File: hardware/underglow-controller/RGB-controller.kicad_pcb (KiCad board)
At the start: 4 copper layers, 86 x 97.7 mm, 175 parts, among them J2 U.FL-R-SMT-1(10), J3 DM3AT-SF-PEJM5, J4 DTM1312PA12PBR008, J5 Conn_01x10, J6 CONSOLE, J7 U.FL-R-SMT-1(10), J8 JTAG, J9 Conn_01x10, Q2 STS8DNF3LL, Q3 STS8DNF3LL, Q4 STS8DNF3LL, Q5 MBT3904DW1T1G, Q6 MBT3904DW1T1G, SW2 SW_Push, SW3 SW_Push, SW4 SW_Push, SW5 SW_Push, U10 DRV8844PWP, U11 RP2040, U2 SX1231HIMLTRT, U3 SN65HVD230, U4 ESP32-S3R2, U5 W25Q128JVS, U6 WS2815B, U7 W25Q128JVS, U8 ADP2303ARDZ-3.3, Y2 40MHZ, Y3 32.7k, Y4 12MHZ, Y5 32.7k

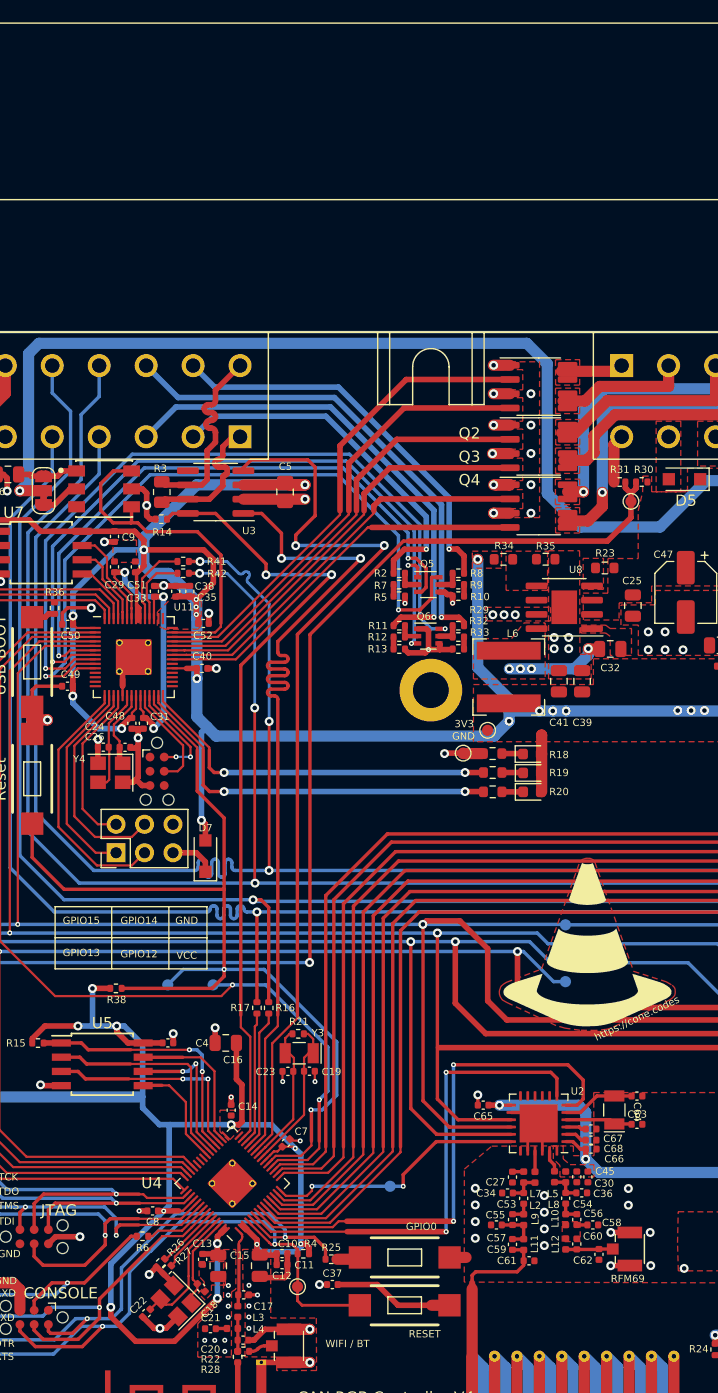
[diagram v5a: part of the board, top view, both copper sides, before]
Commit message: start to break into sheets
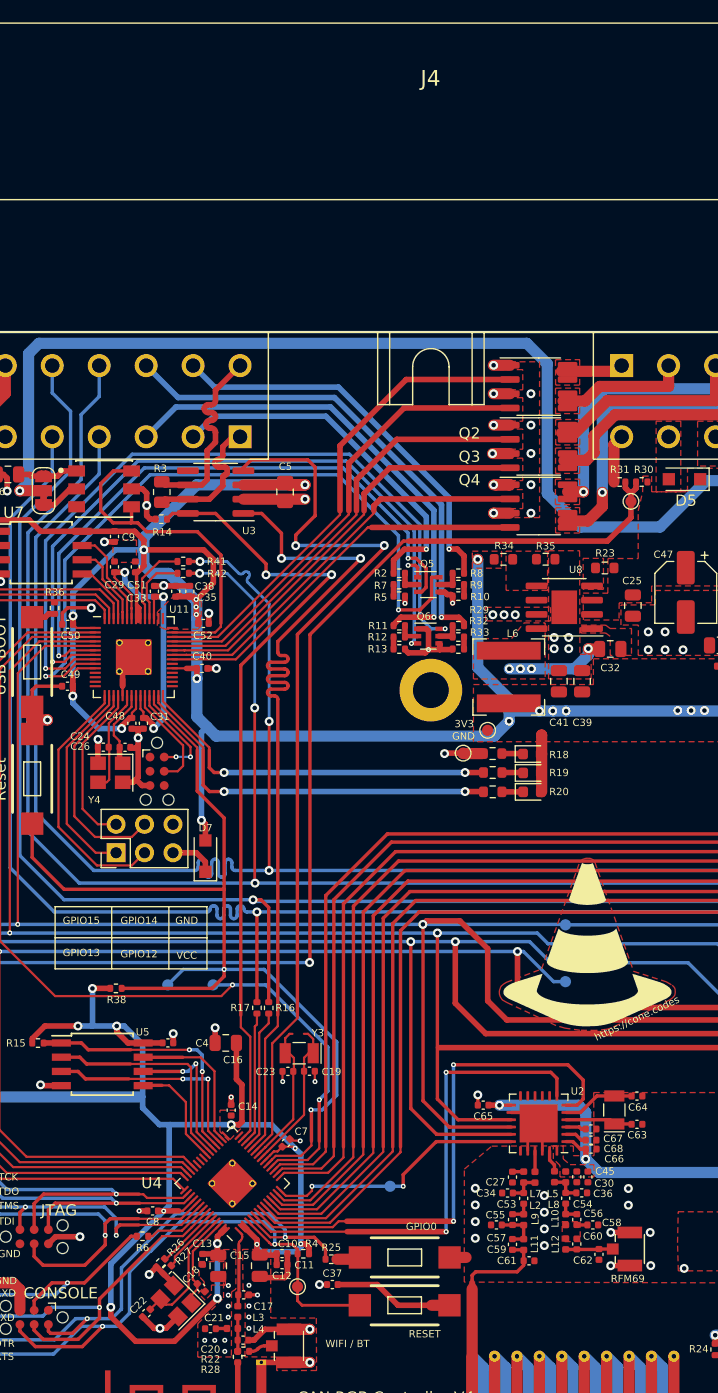
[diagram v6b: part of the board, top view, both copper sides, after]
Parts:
- removed R21: DNP, Resistor_SMD:R_0402_1005Metric
- C38: value 1uF -> 0.1uF
- C51: value 0.1uF -> 1uF
- D3: value RED -> GRN
- D4: value GRN -> RED
- D7: value D_Small -> CUHS15S30,H3F
- J9: value Conn_01x10 -> Spare IO
- SW4: value SW_Push -> USB BOOT
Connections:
- net /LED_GREEN renamed /Pico Remote Proc/LED_GREEN
- net /LED_RED renamed /Pico Remote Proc/LED_RED
- net /RP_GPIO12 renamed /Pico Remote Proc/RP_GPIO12
- net /RP_GPIO13 renamed /Pico Remote Proc/RP_GPIO13
- net /RP_GPIO14 renamed /Pico Remote Proc/RP_GPIO14
- net /RP_GPIO15 renamed /Pico Remote Proc/RP_GPIO15
- net /RP_SCLK renamed /Pico Remote Proc/RP_SCLK
- net /RP_SD0 renamed /Pico Remote Proc/RP_SD0
- net /RP_SD1 renamed /Pico Remote Proc/RP_SD1
- net /RP_SD2 renamed /Pico Remote Proc/RP_SD2
- net /RP_SD3 renamed /Pico Remote Proc/RP_SD3
- net /RP_SS renamed /Pico Remote Proc/RP_SS
- net /RP_SWCLK renamed /Pico Remote Proc/RP_SWCLK
- net /RP_SWD renamed /Pico Remote Proc/RP_SWD
- net /RP_USB_D_M renamed /Pico Remote Proc/RP_USB_D_N
- net /RP_USB_D_P renamed /Pico Remote Proc/RP_USB_D_P
- net /USB_BOOT renamed /Pico Remote Proc/USB_BOOT
- C24 pad 1: /RP_XOUT -> /Pico Remote Proc/RP_XOUT
- C26 pad 1: /RP_XIN -> /Pico Remote Proc/RP_XIN
- D3 pad 1: Net-(D3-Pad1) -> Net-(R20-Pad1)
- D4 pad 1: Net-(D4-Pad1) -> Net-(R19-Pad1)
- R19 pad 1: Net-(D3-Pad1) -> Net-(R19-Pad1)
- R20 pad 1: Net-(D4-Pad1) -> Net-(R20-Pad1)
- U11 pad 20: /RP_XIN -> /Pico Remote Proc/RP_XIN
- U11 pad 21: /RP_XOUT -> /Pico Remote Proc/RP_XOUT
- U11 pad 39: /GPIO_GPO2 -> /GPIO_GPO1
- U11 pad 40: /GPIO_GPO1 -> /GPIO_GPO2
- Y4 pad 1: /RP_XOUT -> /Pico Remote Proc/RP_XIN
- Y4 pad 3: /RP_XIN -> /Pico Remote Proc/RP_XOUT
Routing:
- net /RP_XIN: track 9.21 -> 0.00 mm
- net /Pico Remote Proc/RP_XIN: track 0.00 -> 9.21 mm
- net /RP_XOUT: track 6.62 -> 0.00 mm
- net /Pico Remote Proc/RP_XOUT: track 0.00 -> 6.62 mm
- net Net-(R20-Pad1): track 0.00 -> 3.40 mm
- net /GPIO_GPO2: track 41.4 -> 43.6 mm
- net /GPIO_GPO1: track 43.6 -> 41.4 mm
- net Net-(D4-Pad1): track 1.72 -> 0.00 mm
- net Net-(D3-Pad1): track 1.68 -> 0.00 mm

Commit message: pcb updates
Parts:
- removed C28: 1uF, Capacitor_SMD:C_0402_1005Metric
- removed C68: 0.1uF, Capacitor_SMD:C_0402_1005Metric
- removed D6: D_Small, Diode_SMD:D_SOD-123F
- removed J3: DM3AT-SF-PEJM5, ConeCodes:HRS_DM3AT-SF-PEJM5
- removed J5: Conn_01x10, Connector_PinHeader_2.54mm:PinHeader_1x10_P2.54mm_Vertical
- removed J8: JTAG, Connector_PinHeader_1.27mm:PinHeader_1x05_P1.27mm_Vertical
- removed R24, R40, R43, R44, R45: 10k, Resistor_SMD:R_0402_1005Metric
- removed TC4: TC2030-IDC, Connector:Tag-Connect_TC2030-IDC-NL_2x03_P1.27mm_Vertical
- added C2: 10uF, Capacitor_SMD:C_0805_2012Metric, F.Cu at (82.4, 116.6)
- added C3: 16pF, Capacitor_SMD:C_0402_1005Metric, F.Cu at (80.0, 114.8)
- added J10: U.FL-R-SMT-1(10), ConeCodes:HRS_U.FL-R-SMT-1(10), F.Cu at (96.0, 100.8)
- added REF**: Wuerth_36103305_30x30mm, RF_Shielding:Wuerth_36103305_30x30mm, F.Cu at (84.7, 121.2)
- added TP13: DIO0, TestPoint:TestPoint_Pad_D1.0mm, F.Cu at (72.3, 122.8)
- added TP14: DIO1, TestPoint:TestPoint_Pad_D1.0mm, F.Cu at (73.9, 123.7)
- added TP15: DIO2, TestPoint:TestPoint_Pad_D1.0mm, F.Cu at (72.3, 124.4)
- added TP16: DIO3, TestPoint:TestPoint_Pad_D1.0mm, F.Cu at (73.9, 125.3)
- added TP17: DIO4, TestPoint:TestPoint_Pad_D1.0mm, F.Cu at (72.3, 126.0)
- added TP18: DIO5, TestPoint:TestPoint_Pad_D1.0mm, F.Cu at (73.9, 126.9)
- AE3: value PCB_ANT_RFM69 -> Antenna_Shield
- C27, C30, C36, C45: value C_Small -> 0.1uF
- C34: value C_Small -> 16pF
- C54: value C_Small -> 0.01uF
- C55: value C_Small -> 68pF
- C56, C59: value C_Small -> 8.2pF
- C58: value C_Small -> 22pF
- C62: value C_Small -> 6.8pF
- C63: value 10pF -> 6.8pF
- C64: value 10pF -> C_Small
- C65: value 0.1uF -> C_Small
- C66: value 0.1uF -> 3.3pF
- C67: value 0.1uF -> 5.6pF
- D3: value GRN -> RED
- D4: value RED -> GRN
- L10, L12: value L_Small -> 6.8nH
- L11, L9: value L_Small -> 5.6nH
- L2: value L_Small -> 2.7nH
- L5: value L_Small -> 3.9nH
- L7: value L_Small -> 22nH
- L8: value L_Small -> 33nH
- TP10, TP11, TP12: moved to F.Cu
- TP3: value VBAT_SENSE -> VSENSE
- U2: footprint Package_DFN_QFN:QFN-24-1EP_5x5mm_P0.65mm_EP3.4x3.4mm -> Package_DFN_QFN:QFN-24-1EP_5x5mm_P0.65mm_EP3.4x3.4mm_ThermalVias
- Y5: value 32.7k -> 32mhz; footprint Crystal:Crystal_SMD_MicroCrystal_CC7V-T1A-2Pin_3.2x1.5mm -> Crystal:Crystal_SMD_2520-4Pin_2.5x2.0mm
- moved C65 26.0 mm to (91.5, 127.8)
- moved AE3 25.5 mm to (103.7, 124.0), turned to -90 degrees
- moved J2 24.0 mm to (90.9, 100.7), turned to 0 degrees
- moved C67 18.3 mm to (93.1, 127.1), turned to -90 degrees
- moved L11 16.3 mm to (91.5, 121.9), turned to 0 degrees
- moved C63 14.2 mm to (90.0, 126.2), turned to 90 degrees
- moved C64 14.2 mm to (91.5, 123.0), turned to 180 degrees
- moved C66 14.0 mm to (93.1, 122.5), turned to 90 degrees
- moved L9 13.3 mm to (88.5, 123.0), turned to 0 degrees
- moved C57 13.1 mm to (85.1, 126.2), turned to 90 degrees
- moved C61 13.0 mm to (88.5, 127.7), turned to 180 degrees
- moved L12 12.9 mm to (91.5, 126.6), turned to 0 degrees
- moved AE2 12.9 mm to (36.9, 133.9)
- moved C59 12.7 mm to (86.6, 126.6), turned to 0 degrees
- moved U2 12.6 mm to (79.1, 125.0), turned to -90 degrees
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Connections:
- net /BST renamed /Power/BST
- net /CHIP_PU renamed /ESP32-S3/CHIP_PU
- net /CP1 renamed /Motor-Control/CP1
- net /CP2 renamed /Motor-Control/CP2
- net /DRV_RESET renamed /MCPWM_RESET
- net /DRV_SLEEP renamed /MCPWM_SLEEP
- net /EN1 renamed /MCPWM0_ENA
- net /EN2 renamed /MCPWM0_ENB
- net /EN3 renamed /MCPWM1_ENA
- net /EN4 renamed /MCPWM1_ENB
- net /FB renamed /Power/FB
- net /FSPICLK renamed /SCLK
- net /FSPICS0 renamed /ESP32-S3/FSPICS0
- net /FSPICS1 renamed /CS1
- net /FSPICS2 renamed /CS2
- net /FSPID renamed /MOSI
- net /FSPIQ renamed /MISO
- net /GPI1 renamed /Connectors/GPI1
- net /GPI2 renamed /Connectors/GPI2
- net /GPI3 renamed /Connectors/GPI3
- net /GPI4 renamed /Connectors/GPI4
- net /GPIO0_BOOTSTRAP renamed /ESP32-S3/GPIO0_BOOTSTRAP
- net /GPIO1 renamed /SX1276_IRQ
- net /GPIO10 renamed /MCPWM1_INB
- net /GPIO14 renamed /RP2040_EN
- net /GPIO2 renamed /SX1276_RESET
- net /GPIO21 renamed /CAN_EN
- net /GPIO3 renamed /MCPWM0_INA
- net /GPIO38 renamed /VSENSE
- net /GPIO5 renamed /MCPWM0_INB
- net /GPIO7 renamed /MCPWM1_INA
- net /GPIO_USB_D_N renamed /ESP32-S3/GPIO19
- net /GPIO_USB_D_P renamed /ESP32-S3/GPIO20
- net /GPO1 renamed /Connectors/GPO1
- net /GPO2 renamed /Connectors/GPO2
- net /GPO3 renamed /Connectors/GPO3
- net /GPO4 renamed /Connectors/GPO4
- net /GPO5 renamed /Connectors/GPO5
- net /GPO6 renamed /Connectors/GPO6
- net /LEDA_OUT renamed /External-IO/LEDA_OUT
- net /LNA_IN renamed /ESP32-S3/LNA_IN
- net /MOTOR1_OUT1 renamed /Connectors/MOTOR1_OUT1
- net /MOTOR1_OUT2 renamed /Connectors/MOTOR1_OUT2
- net /PGOOD renamed /Power/PGOOD
- net /RF_ANT renamed /ESP32-S3/RF_ANT
- net /RF_ANT_EXT renamed /ESP32-S3/RF_ANT_EXT
- net /RTC_XTAL_N renamed /ESP32-S3/RTC_XTAL_N
- net /RTC_XTAL_P renamed /ESP32-S3/RTC_XTAL_P
- net /RXD renamed /ESP32-S3/RXD
- net /SPICLK renamed /ESP32-S3/SPICLK
- net /SPICS0 renamed /ESP32-S3/SPICS0
- net /SPICS1 renamed /ESP32-S3/SPICS1
- net /SPID renamed /ESP32-S3/SPID
- net /SPIHD renamed /ESP32-S3/SPIHD
- net /SPIQ renamed /ESP32-S3/SPIQ
- net /SPIWP renamed /ESP32-S3/SPIWP
- net /SW renamed /Power/SW
- net /TXD renamed /ESP32-S3/TXD
- net /WS2815B_VCC renamed /External-IO/WS2815B_VCC
- net /WS2815B_VDD renamed /External-IO/WS2815B_VDD
- net /XTAL_N renamed /ESP32-S3/XTAL_N
- net /XTAL_P renamed /ESP32-S3/XTAL_P
- net Net-(C42-Pad1) renamed /Motor-Control/V3P3OUT
- net Net-(C43-Pad1) renamed /Motor-Control/VCP
- AE3 pad 1: /RF69_RF_ANT_PCB -> unconnected-(AE3-Pad1)
- C27 pad 1: Net-(C27-Pad1) -> +3V3
- C30 pad 1: /VR_PA -> +3V3
- C34 pad 1: Net-(C34-Pad1) -> /SX1276/RADIO_XTAL_N
- C36 pad 1: Net-(C36-Pad1) -> /SX1276/VR_DIG
- C45 pad 1: /VR_PA -> /SX1276/VR_ANA
- C53 pad 1: Net-(C34-Pad1) -> /SX1276/VR_PA
- C53 pad 2: Net-(C53-Pad2) -> GND
- C54 pad 1: Net-(C36-Pad1) -> /SX1276/VR_PA
- C54 pad 2: Net-(C54-Pad2) -> GND
- C55 pad 1: Net-(C53-Pad2) -> /SX1276/VR_PA
- C55 pad 2: Net-(C55-Pad2) -> GND
- C56 pad 1: Net-(C54-Pad2) -> Net-(C56-Pad1)
- C56 pad 2: Net-(C56-Pad2) -> GND
- C57 pad 1: Net-(C55-Pad2) -> Net-(C57-Pad1)
- C58 pad 1: Net-(C56-Pad2) -> Net-(C56-Pad1)
- C58 pad 2: GND -> Net-(C58-Pad2)
- C59 pad 1: Net-(C55-Pad2) -> Net-(C57-Pad1)
- C59 pad 2: /RF69_RF_ANT_PCB -> Net-(C59-Pad2)
- C60 pad 1: Net-(C56-Pad2) -> Net-(C60-Pad1)
- C60 pad 2: /RF69_RF_EXT -> Net-(C58-Pad2)
- C61 pad 1: /RF69_RF_ANT_PCB -> Net-(C61-Pad1)
- C61 pad 2: GND -> Net-(C59-Pad2)
- C62 pad 1: /RF69_RF_EXT -> Net-(C60-Pad1)
- C63 pad 1: /RADIO_XTAL_P -> Net-(C61-Pad1)
- C64 pad 1: /RADIO_XTAL_N -> Net-(C64-Pad1)
- C64 pad 2: GND -> Net-(C60-Pad1)
- C65 pad 1: +3V3 -> Net-(C65-Pad1)
- C65 pad 2: GND -> Net-(C61-Pad1)
- C66 pad 1: +3V3 -> Net-(C64-Pad1)
- C67 pad 1: /VR_DIG -> Net-(C65-Pad1)
- D3 pad 1: Net-(R20-Pad1) -> Net-(D3-Pad1)
- D4 pad 1: Net-(R19-Pad1) -> Net-(D4-Pad1)
- J2 pad 2: /RF69_RF_EXT -> Net-(C64-Pad1)
- J4 pad A10: /MOTOR2_OUT2 -> /Connectors/MOTOR2_OUT2
- J4 pad A9: /MOTOR2_OUT1 -> /Connectors/MOTOR2_OUT1
- J4 pad B4: /CONN_RP_USB_D_P -> unconnected-(J4-PadB4)
- J4 pad B5: /USB_D_P -> unconnected-(J4-PadB5)
- J4 pad B7: /V33OUT -> unconnected-(J4-PadB7)
- J4 pad B8: /USB_D_N -> unconnected-(J4-PadB8)
- J4 pad B9: /CONN_RP_USB_D_N -> unconnected-(J4-PadB9)
- J6 pad 5: /CTS -> /ESP32-S3/CTS
- L10 pad 1: Net-(C54-Pad2) -> Net-(C59-Pad2)
- L10 pad 2: Net-(C56-Pad2) -> Net-(C61-Pad1)
- L11 pad 1: Net-(C55-Pad2) -> Net-(C60-Pad1)
- L11 pad 2: /RF69_RF_ANT_PCB -> Net-(C64-Pad1)
- L12 pad 1: Net-(C56-Pad2) -> Net-(C61-Pad1)
- L12 pad 2: /RF69_RF_EXT -> Net-(C65-Pad1)
- L2 pad 1: /RFIO -> /SX1276/PA_BOOST
- L2 pad 2: Net-(C34-Pad1) -> Net-(C56-Pad1)
- L5 pad 1: /PA_BOOST -> /SX1276/RFIO
- L5 pad 2: Net-(C36-Pad1) -> Net-(C57-Pad1)
- L7 pad 1: Net-(C27-Pad1) -> /SX1276/VR_PA
- L7 pad 2: Net-(C34-Pad1) -> Net-(C56-Pad1)
- L8 pad 1: /VR_PA -> /SX1276/VR_PA
- L8 pad 2: Net-(C36-Pad1) -> Net-(C57-Pad1)
- L9 pad 1: Net-(C53-Pad2) -> Net-(C58-Pad2)
- L9 pad 2: Net-(C55-Pad2) -> Net-(C60-Pad1)
- R16 pad 2: /USB_D_N -> /Connectors/USB_D_P
- R17 pad 2: /USB_D_P -> /Connectors/USB_D_N
- R19 pad 1: Net-(R19-Pad1) -> Net-(D3-Pad1)
- R20 pad 1: Net-(R20-Pad1) -> Net-(D4-Pad1)
- R25 pad 1: /CTS -> /ESP32-S3/CTS
- R26 pad 1: /GPIO45 -> /ESP32-S3/GPIO45
- R27 pad 1: /GPIO46 -> /ESP32-S3/GPIO46
- R41 pad 1: /CONN_RP_USB_D_P -> /Connectors/CONN_RP_USB_D_P
- R42 pad 1: /CONN_RP_USB_D_N -> /Connectors/CONN_RP_USB_D_N
- TC2 pad 2: /CTS -> /ESP32-S3/CTS
- U10 pad 10: /MOTOR2_OUT2 -> /Connectors/MOTOR2_OUT1
- U10 pad 18: unconnected-(U10-Pad18) -> /MCPWM_FAULT
- U10 pad 8: /MOTOR2_OUT1 -> /Connectors/MOTOR2_OUT2
- U11 pad 39: /GPIO_GPO1 -> /GPIO_GPO2
- U11 pad 40: /GPIO_GPO2 -> /GPIO_GPO1
- U2 pad 10: unconnected-(U2-Pad10) -> /SX1276/DIO3
- U2 pad 11: unconnected-(U2-Pad11) -> /SX1276/DIO4
- U2 pad 12: unconnected-(U2-Pad12) -> /SX1276/DIO5
- U2 pad 2: /VR_ANA -> /SX1276/VR_ANA
- U2 pad 21: /RFIO -> /SX1276/RFIO
- U2 pad 23: /PA_BOOST -> /SX1276/PA_BOOST
- U2 pad 24: /VR_PA -> /SX1276/VR_PA
- U2 pad 3: /VR_DIG -> /SX1276/VR_DIG
- U2 pad 4: /RADIO_XTAL_P -> /SX1276/RADIO_XTAL_P
- U2 pad 5: /RADIO_XTAL_N -> /SX1276/RADIO_XTAL_N
- U2 pad 8: unconnected-(U2-Pad8) -> /SX1276/DIO1
- U2 pad 9: unconnected-(U2-Pad9) -> /SX1276/DIO2
- U4 pad 44: /MTCK -> /ESP32-S3/MTCK
- U4 pad 45: /MTDO -> /ESP32-S3/MTDO
- U4 pad 47: /MTDI -> /ESP32-S3/MTDI
- U4 pad 48: /MTMS -> /ESP32-S3/MTMS
- U4 pad 5: /CTS -> unconnected-(U4-Pad5)
- U4 pad 51: /GPIO45 -> unconnected-(U4-Pad51)
- U4 pad 52: /GPIO46 -> unconnected-(U4-Pad52)
- Y5 pad 1: /RADIO_XTAL_P -> /SX1276/RADIO_XTAL_P
- Y5 pad 2: /RADIO_XTAL_N -> GND
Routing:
- net /Connectors/USB_D_N: track 0.00 -> 268.7 mm, vias 0 -> 2
- net /Connectors/CONN_RP_USB_D_P: track 0.00 -> 153.1 mm, vias 0 -> 3
- net /CONN_RP_USB_D_P: track 153.1 -> 0.00 mm, vias 3 -> 0
- net /Connectors/CONN_RP_USB_D_N: track 0.00 -> 152.7 mm, vias 0 -> 3
- net /CONN_RP_USB_D_N: track 152.7 -> 0.00 mm, vias 3 -> 0
- net /USB_D_N: track 136.0 -> 0.00 mm, vias 1 -> 0
- net /USB_D_P: track 132.7 -> 0.00 mm, vias 1 -> 0
- net +3V3: track 509.6 -> 422.5 mm, vias 37 -> 30
- net /MISO: track 232.0 -> 167.3 mm, vias 3 -> 2
- net /MOSI: track 232.4 -> 168.5 mm, vias 5 -> 1
- net /SCLK: track 218.1 -> 166.7 mm, vias 3 -> 2
- net /CTS: track 48.6 -> 0.00 mm, vias 2 -> 0
- net /ESP32-S3/FSPICS0: track 134.5 -> 86.3 mm, vias 2 -> 1
- net (no net): track 0.00 -> 40.2 mm
- net /MTDI: track 32.3 -> 0.00 mm, vias 1 -> 0
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- added copper zone on F.Cu, net /Connectors/MOTOR2_OUT1
- added copper zone on F.Cu, net /Connectors/MOTOR2_OUT2
- removed copper zone on F.Cu, net /MOTOR2_OUT1
- removed copper zone on F.Cu, net /MOTOR2_OUT2
- removed copper zone on F.Cu, net /VR_PA
- removed copper zone on F.Cu, net Net-(C56-Pad2)
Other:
- outline, holes or cut-outs redrawn
- board text removed: "JLCJLCJLCJLC"
- board text removed: "JTAG"
- board text removed: "RFM69"
- board text removed: "TCK"
- board text removed: "TDI"
- board text removed: "TDO"
- board text removed: "TMS"

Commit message: i can't believe what they did to my boy
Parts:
- removed C19, C23: 10pF, Capacitor_SMD:C_0402_1005Metric
- removed C6: 0.1uF, Capacitor_SMD:C_0805_2012Metric
- removed H1: MountingHole_Pad, MountingHole:MountingHole_3.2mm_M3_DIN965_Pad
- removed J9: Spare IO, Connector_PinHeader_2.54mm:PinHeader_2x03_P2.54mm_Vertical
- removed JP2: LED Voltage Select, Jumper:SolderJumper-3_P1.3mm_Bridged12_RoundedPad1.0x1.5mm_NumberLabels
- removed Q4: STS8DNF3LL, Package_SO:SO-8_3.9x4.9mm_P1.27mm
- removed REF**: Wuerth_36103305_30x30mm, RF_Shielding:Wuerth_36103305_30x30mm
- removed TC3: TC2030-IDC, Connector:Tag-Connect_TC2030-IDC-NL_2x03_P1.27mm_Vertical
- removed TP10: CS1, TestPoint:TestPoint_Pad_D1.0mm
- removed TP11: CS2, TestPoint:TestPoint_Pad_D1.0mm
- removed TP12: RP_RUN, TestPoint:TestPoint_Pad_D1.0mm
- removed TP2: CHIP_PU, TestPoint:TestPoint_Pad_D1.0mm
- removed TP5: MOSI, TestPoint:TestPoint_Pad_D1.0mm
- removed TP6: MISO, TestPoint:TestPoint_Pad_D1.0mm
- removed TP8: SCLK, TestPoint:TestPoint_Pad_D1.0mm
- removed TP9: CS0, TestPoint:TestPoint_Pad_D1.0mm
- removed U6: WS2815B, ConeCodes:worldsemi-WS2815B-MFG
- removed Y3: 32.7k, Crystal:Crystal_SMD_MicroCrystal_CC7V-T1A-2Pin_3.2x1.5mm
- added AE4: Antenna_Shield, RF_Antenna:Texas_SWRA416_868MHz_915MHz, F.Cu at (102.6, 86.3)
- added D6: GRN, LED_SMD:LED_0603_1608Metric, F.Cu at (148.8, 91.1)
- added D8: PESD2CANFD24V-T, Package_TO_SOT_SMD:SOT-23, F.Cu at (10.9, 48.7)
- added D9: GRN, LED_SMD:LED_0603_1608Metric, F.Cu at (115.0, 72.1)
- added F2: Fuse, ConeCodes:Keystone-3587-10TR, F.Cu at (62.6, 56.4)
- added J3: Conn_01x04, Connector_PinHeader_1.27mm:PinHeader_1x04_P1.27mm_Vertical, F.Cu at (47.6, 61.1)
- added J5: Conn_01x10, Connector_PinHeader_2.54mm:PinHeader_1x10_P2.54mm_Vertical, F.Cu at (53.8, 110.8)
- added Q7: Q_PMOS_GDS, Package_TO_SOT_SMD:TO-252-2, F.Cu at (87.1, 59.5)
- added R21: 240R, Resistor_SMD:R_0603_1608Metric, F.Cu at (148.8, 94.2)
- added R24: 0R, Resistor_SMD:R_0402_1005Metric, F.Cu at (93.6, 99.4)
- added R40: 0R, Resistor_SMD:R_0402_1005Metric, F.Cu at (93.1, 103.0)
- added R43: 0R, Resistor_SMD:R_0402_1005Metric, F.Cu at (93.6, 95.7)
- added R44: 0R, Resistor_SMD:R_0402_1005Metric, F.Cu at (93.1, 95.2)
- added R45: 0R, Resistor_SMD:R_2512_6332Metric, F.Cu at (133.5, 55.6)
- added R46: 240R, Resistor_SMD:R_0603_1608Metric, F.Cu at (119.0, 72.1)
- added R47: 10k, Resistor_SMD:R_0603_1608Metric, F.Cu at (133.2, 78.3)
- added R48: 10k, Resistor_SMD:R_0603_1608Metric, F.Cu at (85.4, 66.7)
- D7: value CUHS15S30,H3F -> PESD2CANFD24V-T; footprint Diode_SMD:D_SOD-123F -> Package_TO_SOT_SMD:SOT-23
- R39: footprint Resistor_SMD:R_0402_1005Metric -> Resistor_SMD:R_0603_1608Metric
- moved G*** 84.3 mm to (-10.2, 81.2)
- moved R18 76.0 mm to (147.1, 94.2), turned to -90 degrees
- moved D2 72.0 mm to (147.1, 91.1), turned to 90 degrees
- moved TP3 57.6 mm to (141.7, 66.4)
- moved R30 57.6 mm to (142.7, 64.7)
- moved R31 57.6 mm to (140.7, 64.7)
- moved R3 36.4 mm to (7.40, 48.7), turned to 90 degrees
- moved D7 35.4 mm to (35.3, 55.4), turned to -90 degrees
- moved D4 32.2 mm to (43.9, 80.6), turned to 180 degrees
- moved D3 32.1 mm to (43.9, 82.3), turned to 180 degrees
- moved C58 26.8 mm to (88.7, 96.2)
- moved C61 26.8 mm to (89.6, 100.9)
- moved L10 26.8 mm to (89.6, 99.9)
- moved R22 26.4 mm to (49.2, 108.9), turned to 0 degrees
- moved C37 26.3 mm to (64.2, 100.1), turned to 0 degrees
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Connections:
- AE3 pad 1: unconnected-(AE3-Pad1) -> Net-(AE3-Pad1)
- C43 pad 2: /VIN -> /Motor-Control/VM
- C44 pad 1: /VIN -> /Motor-Control/VM
- C47 pad 1: /VIN -> /Motor-Control/VM
- D5 pad 2: /VBAT -> /Connectors/VBAT
- D7 pad 1: Net-(D7-Pad1) -> /Connectors/USB_D_P
- D7 pad 2: +3V3 -> /Connectors/USB_D_N
- J10 pad 2: Net-(C65-Pad1) -> Net-(J10-Pad2)
- J2 pad 2: Net-(C64-Pad1) -> Net-(J2-Pad2)
- J4 pad A11: /VBAT -> unconnected-(J4-PadA11)
- J4 pad A12: GND -> /Connectors/FUSE_IN
- J4 pad A4: /Connectors/GPO4 -> /Connectors/VOUT
- J4 pad A5: /Connectors/GPO6 -> unconnected-(J4-PadA5)
- J4 pad A6: /Connectors/GPO5 -> unconnected-(J4-PadA6)
- J4 pad B1: /CAN_P -> /CAN_N
- J4 pad B12: /CAN_N -> /CAN_P
- J4 pad B4: unconnected-(J4-PadB4) -> /Connectors/USB_D_P
- J4 pad B5: unconnected-(J4-PadB5) -> /Connectors/USB_D_N
- Q3 pad 5: /Connectors/GPO4 -> /External-IO/GPO4
- Q3 pad 6: /Connectors/GPO4 -> /External-IO/GPO4
- R39 pad 1: +3V3 -> /Motor-Control/V3P3OUT
- U10 pad 10: /Connectors/MOTOR2_OUT1 -> /Connectors/MOTOR2_OUT2
- U10 pad 11: /VIN -> /Motor-Control/VM
- U10 pad 4: /VIN -> /Motor-Control/VM
- U10 pad 8: /Connectors/MOTOR2_OUT2 -> /Connectors/MOTOR2_OUT1
- U11 pad 15: /Pico Remote Proc/RP_GPIO12 -> unconnected-(U11-Pad15)
- U11 pad 16: /Pico Remote Proc/RP_GPIO13 -> unconnected-(U11-Pad16)
- U11 pad 17: /Pico Remote Proc/RP_GPIO14 -> unconnected-(U11-Pad17)
- U11 pad 18: /Pico Remote Proc/RP_GPIO15 -> unconnected-(U11-Pad18)
- U11 pad 24: /Pico Remote Proc/RP_SWCLK -> unconnected-(U11-Pad24)
- U11 pad 25: /Pico Remote Proc/RP_SWD -> unconnected-(U11-Pad25)
- U11 pad 29: unconnected-(U11-Pad29) -> /GPIO_GPI4
- U11 pad 30: unconnected-(U11-Pad30) -> /GPIO_GPI3
- U11 pad 31: unconnected-(U11-Pad31) -> /GPIO_GPI2
- U11 pad 32: unconnected-(U11-Pad32) -> /GPIO_GPI1
- U11 pad 6: /GPIO_GPI1 -> unconnected-(U11-Pad6)
- U11 pad 7: /GPIO_GPI3 -> unconnected-(U11-Pad7)
- U11 pad 8: /GPIO_GPI4 -> unconnected-(U11-Pad8)
- U11 pad 9: /GPIO_GPI2 -> unconnected-(U11-Pad9)
- U4 pad 14: /CS1 -> unconnected-(U4-Pad14)
- U4 pad 18: /CS2 -> /VSENSE
- U4 pad 23: /GPIO_CAN_N -> /GPIO_CAN_P
- U4 pad 24: /GPIO_CAN_P -> /GPIO_CAN_N
- U4 pad 38: unconnected-(U4-Pad38) -> /CS2
- U4 pad 39: /ESP32-S3/FSPICS0 -> /ESP32-S3/GPIO34
- U4 pad 43: /VSENSE -> unconnected-(U4-Pad43)
- U4 pad 5: unconnected-(U4-Pad5) -> /CS1
- U4 pad 6: /SX1276_IRQ -> /SX1276_RESET
- U4 pad 7: /SX1276_RESET -> /SX1276_IRQ
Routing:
- net +3V3: track 422.5 -> 95.4 mm, vias 30 -> 35
- net /Connectors/USB_D_N: track 268.7 -> 42.0 mm
- net /Connectors/CONN_RP_USB_D_P: track 153.1 -> 2.24 mm, vias 3 -> 1
- net /Connectors/CONN_RP_USB_D_N: track 152.7 -> 2.25 mm, vias 3 -> 1
- net /VSENSE: track 134.2 -> 29.9 mm, vias 2 -> 0
- net /VIN: track 93.7 -> 0.00 mm, vias 13 -> 0
- net /ESP32-S3/FSPICS0: track 86.3 -> 0.00 mm, vias 1 -> 0
- net GND: track 120.3 -> 205.4 mm, vias 71 -> 184
- net /GPIO_CAN_P: track 79.1 -> 0.00 mm, vias 2 -> 0
- net /MOSI: track 168.5 -> 104.4 mm, vias 1 -> 3
- net /SCLK: track 166.7 -> 106.9 mm, vias 2 -> 4
- net /GPIO_CAN_N: track 81.8 -> 22.4 mm, vias 2 -> 0
- net /MISO: track 167.3 -> 108.3 mm, vias 2 -> 4
- net /CAN_EN: track 72.2 -> 19.8 mm, vias 2 -> 0
- net /GPIO_GPO1: track 43.6 -> 0.00 mm
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- added copper zone on In2.Cu, net +3V3
- added copper zone on F.Cu, net /External-IO/GPO4
- added copper zone on B.Cu, net /Motor-Control/VM
- added copper zone on F.Cu, net /Motor-Control/VM
- added copper zone on In2.Cu, net /Motor-Control/VM
- removed copper zone on F.Cu, net /Connectors/GPO4
- removed copper zone on F.Cu, net /Connectors/GPO5
- removed copper zone on F.Cu, net /Connectors/GPO6
- removed copper zone on F.Cu, net /VBAT
- removed copper zone on B.Cu, net /VIN
- removed copper zone on In2.Cu, net /VIN
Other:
- board text removed: "CS0"
- board text removed: "CS2"
- board text removed: "ESP D+"
- board text removed: "ESP D-"
- board text removed: "GPIO12"
- board text removed: "GPIO13"
- board text removed: "GPIO14"
- board text removed: "GPIO15"
- board text removed: "MISO"
- board text removed: "MOSI"
- board text removed: "RP D+"
- board text removed: "RP D-"
- board text removed: "RP2040 RUN"
- board text removed: "SCLK"
- board text removed: "VCC"
- board text removed: "WIFI / BT"
